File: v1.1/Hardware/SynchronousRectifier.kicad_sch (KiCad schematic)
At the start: 15 parts, among them J1 MAINS_IN, U1 4N39, U2 4N39

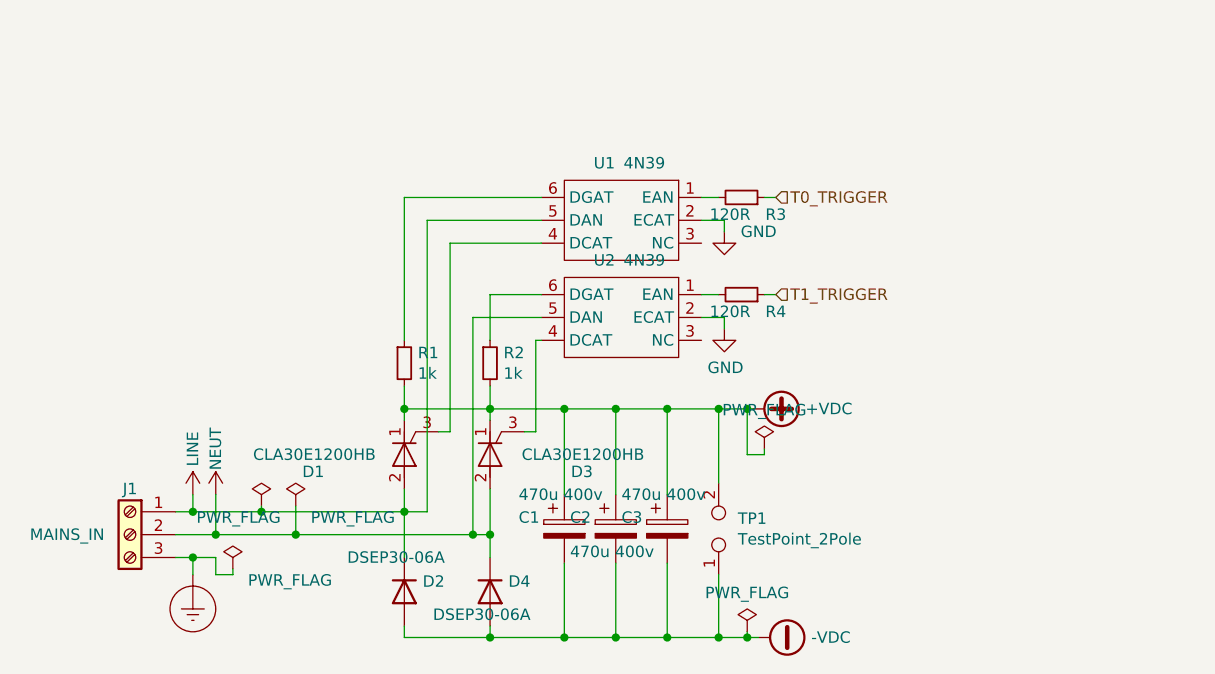
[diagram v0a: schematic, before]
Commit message: v1.1&v1.2 PCB addition.
#####v1.1#####
+Change of MCU; STM32F334C8T6 instead of STM32F103C8T6.
+Filtering 3rd order components of the square wave.
+Use  4 capacitors.
+Adapted to generic transformer(primary 6.4mH, secondary 14.4mH)
+Faster IGBT.

########v1.2#######
+Measures only PZT current and voltage.
+Differential inputs.
+Analog circuitry is capable of measuring four quadrant voltage, current and complex impedance.
+Half bridge configuration.
+Gate resistance of the IGBT's lowered.
+Only USART based touch panel can be connected; not conventional LCD.
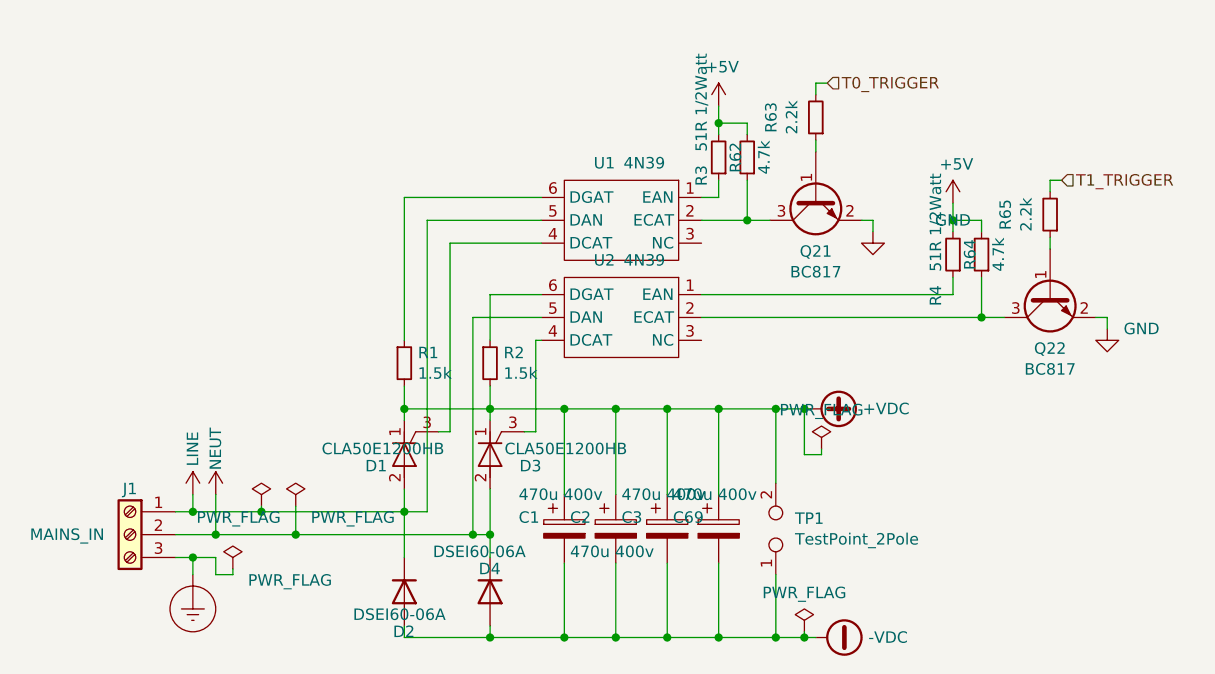
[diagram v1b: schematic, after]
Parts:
- added C69: 470u 400v, oe_capacitor:CP_Radial_D35.0mm_P10.00mm_SnapIn, symbol Device:CP
- added Q21, Q22: BC817, Package_TO_SOT_SMD:SOT-23, symbol Transistor_BJT:BC817
- added R62, R64: 4.7k, Resistor_SMD:R_0805_2012Metric, symbol Device:R_Small
- added R63, R65: 2.2k, Resistor_SMD:R_0805_2012Metric, symbol Device:R_Small
- D1, D3: value CLA30E1200HB -> CLA50E1200HB; Link https://ozdisan.com/power-semiconductors/thyristors/discrete-thyristors/CLA30E1200HB -> https://ozdisan.com/power-semiconductors/thyristors/discrete-thyristors/CLA50E1200HB; Price 12.26508TL -> 13.43667TL
- D2, D4: value DSEP30-06A -> DSEI60-06A; Link https://ozdisan.com/power-semiconductors/diodes-diode-modules-and-rectifiers/general-purpose-diodes/DSEP30-06A -> https://ozdisan.com/power-semiconductors/diodes-diode-modules-and-rectifiers/general-purpose-diodes/DSEI60-06A; Price 10.48412TL -> 20.69234TL
- R1, R2: value 1k -> 1.5k; footprint Resistor_THT:R_Axial_DIN0204_L3.6mm_D1.6mm_P5.08mm_Horizontal -> Resistor_THT:R_Axial_DIN0204_L3.6mm_D1.6mm_P7.62mm_Horizontal; Link https://ozdisan.com/passive-components/resistors/tht-through-hole-resistors/CFR0W8J0102A50 -> https://ozdisan.com/passive-components/resistors/tht-through-hole-resistors/CFR0W8J0152A50; Price 0.03898TL -> 0.01961TL
- R3, R4: value 120R -> 51R 1/2Watt; footprint Resistor_THT:R_Axial_DIN0207_L6.3mm_D2.5mm_P10.16mm_Horizontal -> Resistor_SMD:R_1210_3225Metric; Link https://ozdisan.com/passive-components/resistors/tht-throug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 -> https://ozdisan.com/passive-components/resistors/smt-smd-an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; Price 0.04784TL -> 0.13383TL
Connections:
- net +VDC: now also C69.1
- net -VDC: now also C69.2
- net GND: now also Q21.2 (E), Q22.2 (E); no longer U1.2 (ECAT), U2.2 (ECAT)
- net T0_TRIGGER: now also R63.2; no longer R3.1
- net T1_TRIGGER: now also R65.2; no longer R4.1
- net at U1.1 (EAN): now also R3.1; no longer R3.2
- net at U2.1 (EAN): now also R4.1; no longer R4.2
- new net: Q21.1 (B), R63.1
- new net: Q22.1 (B), R65.1
- new net: Q21.3 (C), R62.1, U1.2 (ECAT)
- new net: Q22.3 (C), R64.1, U2.2 (ECAT)
- new net +5V: R3.2, R4.2, R62.2, R64.2
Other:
- moved on the sheet: TP1
